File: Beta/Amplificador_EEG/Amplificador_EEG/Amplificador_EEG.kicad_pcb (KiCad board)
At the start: 2 copper layers, 51.4 x 56.7 mm, 49 parts, among them J1 IN, J2 REF, J3 GND, J4 POWER, J5 OUTPUT, U1 LM358, U2 AD620, U3 LM358, U4 LM358, U5 LM358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

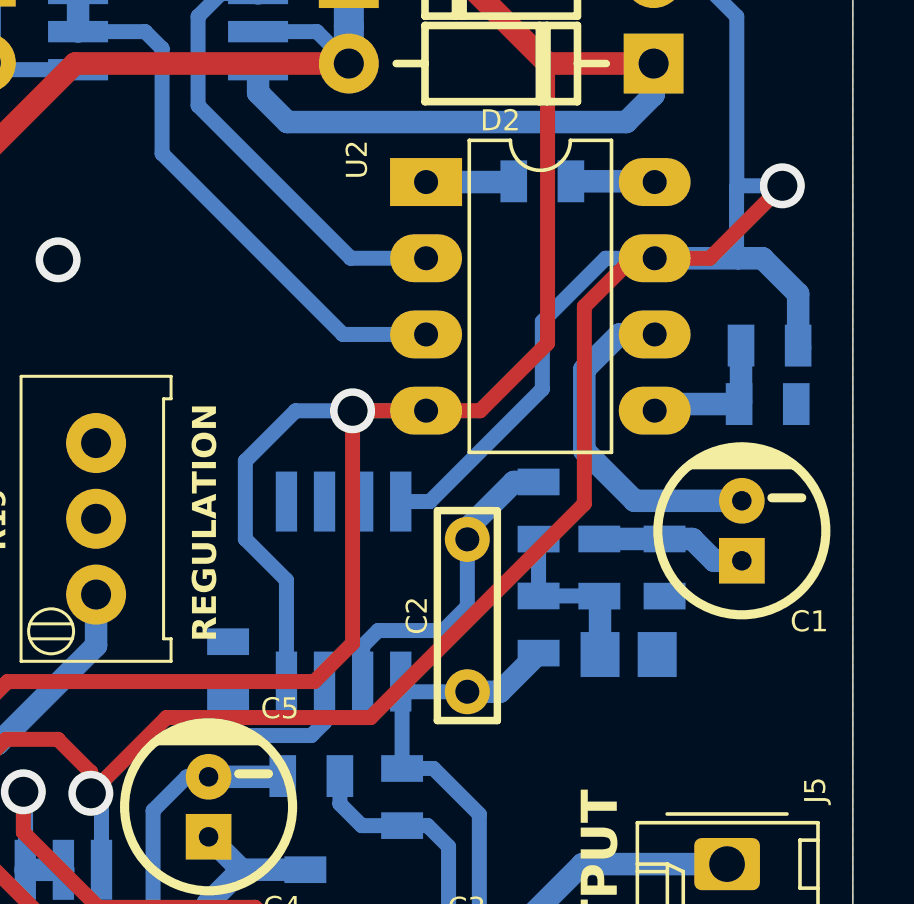
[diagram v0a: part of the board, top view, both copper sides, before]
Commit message: Actualización Componentes PCBs
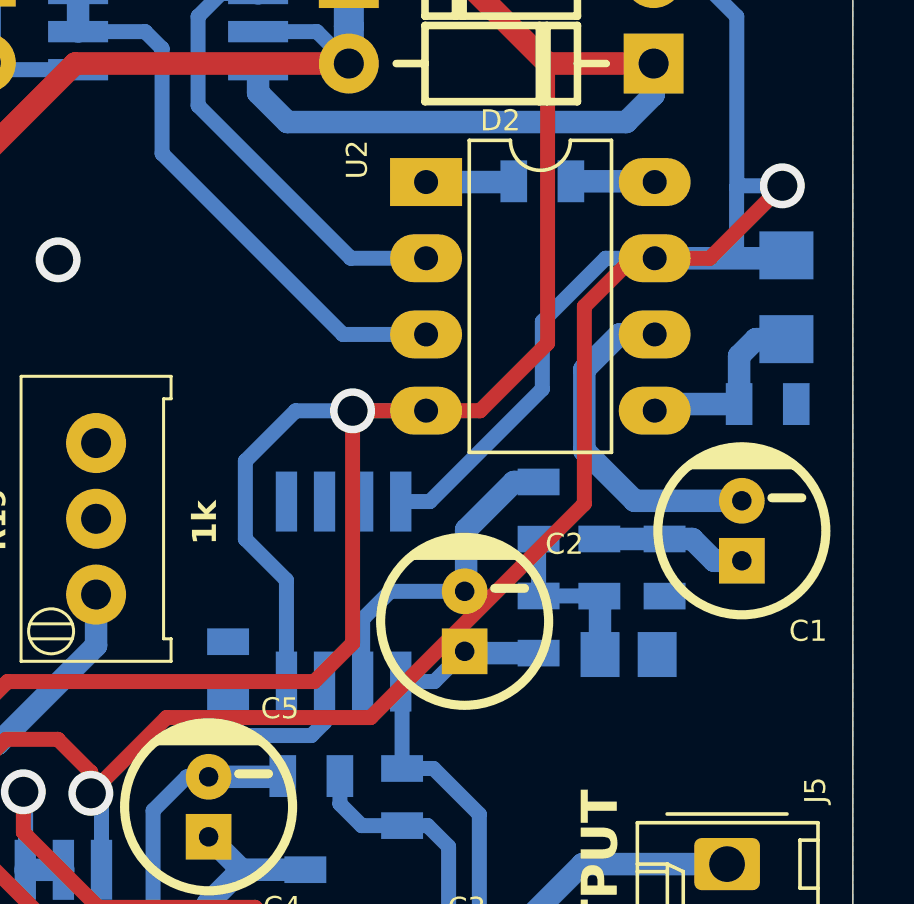
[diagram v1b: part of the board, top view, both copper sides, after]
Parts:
- C2: footprint EESTN5:CAP_0.2 -> EESTN5:CAP_ELEC_5x11mm
- R19: value REGULATION -> 1k
- R2: footprint EESTN5:R_0805 -> EESTN5:R_1206
- moved R2 1.71 mm to (177.1, 82.2), turned to 90 degrees
- moved C2 0.21 mm to (166.3, 93.0), turned to 0 degrees
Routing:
- net /AD620_Ref: track 4.88 -> 6.32 mm
- net +5V: track 168.2 -> 167.1 mm

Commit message: Actualización Amplificador
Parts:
- added J6: Mounting Hole, EESTN5:hole_3mm, F.Cu at (153.3, 81.0)
- R2: footprint EESTN5:R_1206 -> EESTN5:RES0.3; moved to F.Cu
- R26: footprint EESTN5:R_0805 -> EESTN5:RES0.3; moved to F.Cu
- moved R26 7.99 mm to (161.5, 117.5), turned to 90 degrees
- moved R2 2.90 mm to (177.2, 79.3), turned to -90 degrees
- moved R27 2.52 mm to (156.8, 111.5), turned to 90 degrees
- moved R17 1.32 mm to (149.1, 111.0)
- moved R16 1.17 mm to (152.1, 110.1)
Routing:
- net +5V: track 167.1 -> 173.3 mm, vias 5 -> 3
- net /Offset_Ref: track 4.22 -> 7.98 mm
- net Net-(U4-IN1-): track 4.05 -> 5.02 mm
- net /NotchFilter_OUT: track 15.6 -> 14.8 mm
- net /AD620_Ref: track 6.32 -> 6.98 mm
- net GND: vias 7 -> 6
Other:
- board size 51.4 x 56.7 mm -> 52.1 x 59.1 mm
